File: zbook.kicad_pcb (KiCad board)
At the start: 2 copper layers, 157 parts, among them J1 USB_C_Receptacle_USB2.0_16P, J2 B2B-XH-A, J3 USB_C_Receptacle_USB2.0_16P, J4 Conn_01x03_Pin, J5 Conn_01x05_Pin, J6 MSD-4-A, J7 DISPLAY CONN, Q1 Q_NMOS_GSD, Q2 SL2301S, Q3 T2N7002AK,LM, SW1 SW_SPDT, SW2 SW_SPST, SW3 SW_SPST, SW4 SW_Push, SW5 SW_Push, SW6 SW_Push, SW7 SW_Push, U3 RP2040, U5 W25Q16JVSS, U6 W25Q16JVSS, U7 TSDP343xx, U8 GSDA213, Y1 12MHz/10pF, Y2 12MHz/10pF

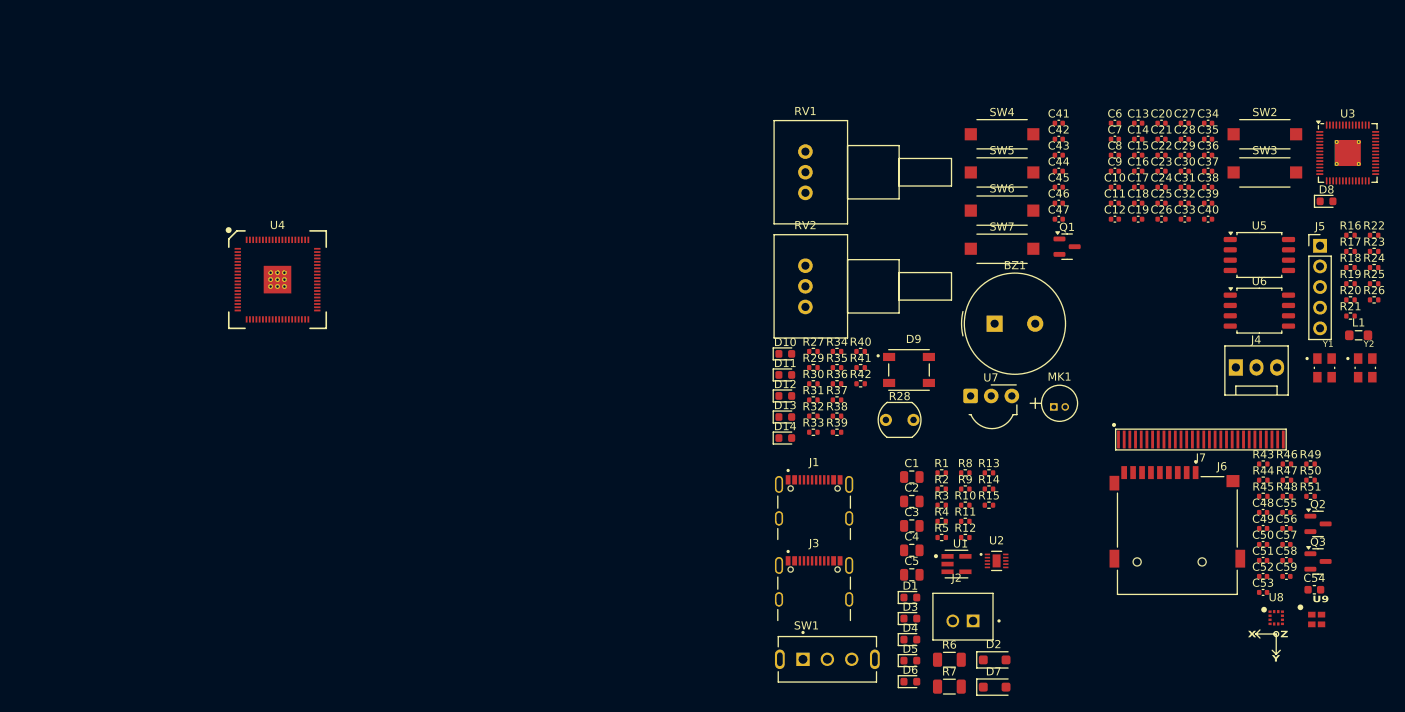
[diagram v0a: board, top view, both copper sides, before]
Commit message: feat: adds testpoints
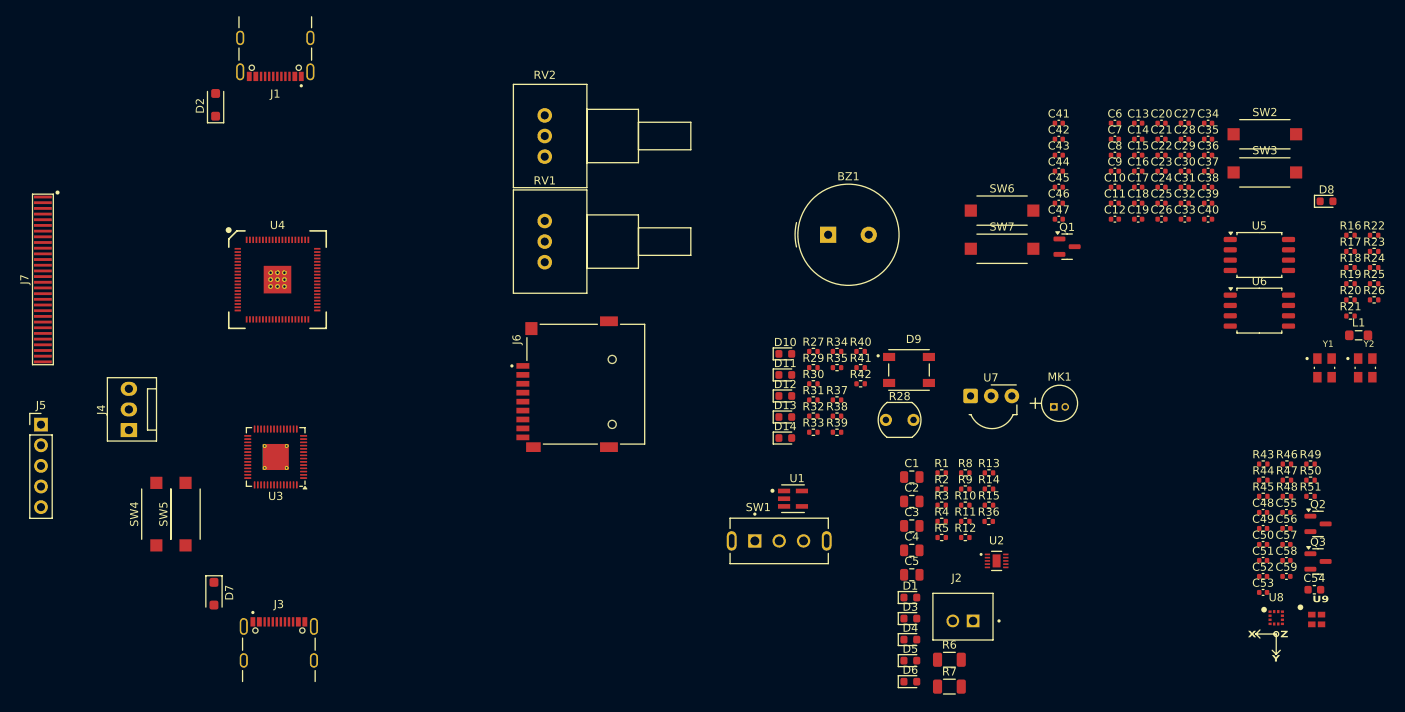
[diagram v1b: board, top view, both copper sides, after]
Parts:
- moved J5 159.0 mm to (111.8, 106.6)
- moved J7 143.9 mm to (112.0, 88.7), turned to -90 degrees
- moved U3 137.2 mm to (140.7, 110.6), turned to 180 degrees
- moved J4 136.5 mm to (122.6, 107.2), turned to 90 degrees
- moved D2 117.8 mm to (133.3, 67.2), turned to 90 degrees
- moved SW4 114.2 mm to (126.0, 117.6), turned to 90 degrees
- moved SW5 109.0 mm to (129.6, 117.6), turned to 90 degrees
- moved D7 96.8 mm to (133.1, 127.4), turned to -90 degrees
- moved J1 92.4 mm to (140.7, 56.4), turned to 180 degrees
- moved J6 75.2 mm to (178.9, 101.6), turned to 90 degrees
- moved J3 66.3 mm to (141.1, 138.2)
- moved RV2 37.1 mm to (173.8, 73.6)
- moved RV1 33.2 mm to (173.8, 86.6)
- moved R36 25.2 mm to (228.5, 118.5)
- moved BZ1 23.2 mm to (208.7, 83.2)
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
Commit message: wip: moves components around on PCB
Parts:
- added J6: Conn_02x10_Counter_Clockwise, Connector_PinSocket_2.54mm:PinSocket_2x10_P2.54mm_Vertical, F.Cu at (230.0, 122.5)
- added TP1: TestPoint_Small, TestPoint:TestPoint_Pad_D1.0mm, F.Cu at (331.6, 149.3)
- added TP10: TestPoint_Small, TestPoint:TestPoint_Pad_D1.0mm, F.Cu at (326.6, 155.4)
- added TP11: TestPoint_Small, TestPoint:TestPoint_Pad_D1.0mm, F.Cu at (326.6, 158.4)
- added TP12: TestPoint_Small, TestPoint:TestPoint_Pad_D1.0mm, F.Cu at (339.8, 163.5)
- added TP13: TestPoint_Small, TestPoint:TestPoint_Pad_D1.0mm, F.Cu at (331.6, 163.5)
- added TP14: TestPoint_Small, TestPoint:TestPoint_Pad_D1.0mm, F.Cu at (331.6, 166.6)
- added TP15: TestPoint_Small, TestPoint:TestPoint_Pad_D1.0mm, F.Cu at (331.6, 169.6)
- added TP16: TestPoint_Small, TestPoint:TestPoint_Pad_D1.0mm, F.Cu at (331.6, 172.7)
- added TP17: TestPoint_Small, TestPoint:TestPoint_Pad_D1.0mm, F.Cu at (334.7, 163.5)
- added TP18: TestPoint_Small, TestPoint:TestPoint_Pad_D1.0mm, F.Cu at (334.7, 166.6)
- added TP19: TestPoint_Small, TestPoint:TestPoint_Pad_D1.0mm, F.Cu at (334.7, 169.6)
- added TP2: TestPoint_Small, TestPoint:TestPoint_Pad_D1.0mm, F.Cu at (331.6, 152.3)
- added TP3: TestPoint_Small, TestPoint:TestPoint_Pad_D1.0mm, F.Cu at (331.6, 155.4)
- added TP4: TestPoint_Small, TestPoint:TestPoint_Pad_D1.0mm, F.Cu at (331.6, 158.4)
- added TP5: TestPoint_Small, TestPoint:TestPoint_Pad_D1.0mm, F.Cu at (334.7, 149.3)
- added TP6: TestPoint_Small, TestPoint:TestPoint_Pad_D1.0mm, F.Cu at (334.7, 152.3)
- added TP7: TestPoint_Small, TestPoint:TestPoint_Pad_D1.0mm, F.Cu at (334.7, 155.4)
- added TP8: TestPoint_Small, TestPoint:TestPoint_Pad_D1.0mm, F.Cu at (326.6, 149.3)
- added TP9: TestPoint_Small, TestPoint:TestPoint_Pad_D1.0mm, F.Cu at (326.6, 152.3)
- moved U8 162.1 mm to (108.2, 85.3)
- moved U9 158.1 mm to (119.5, 78.8), turned to 180 degrees
- moved J2 135.2 mm to (122.8, 42.2)
- moved R7 134.7 mm to (124.2, 48.0), turned to 180 degrees
- moved U6 132.4 mm to (132.0, 66.5), turned to 90 degrees
- moved R6 130.3 mm to (124.2, 51.3), turned to 180 degrees
- moved U2 125.0 mm to (124.4, 55.7)
- moved SW1 123.5 mm to (109.7, 39.8)
- moved Y1 122.9 mm to (147.0, 101.0), turned to 90 degrees
- moved SW2 119.9 mm to (147.5, 104.8)
- moved SW7 119.2 mm to (118.2, 125.8)
- moved U1 118.7 mm to (108.5, 45.8), turned to 180 degrees
- moved U5 117.4 mm to (152.0, 127.2), turned to -90 degrees
- moved R5 112.7 mm to (138.1, 46.0), turned to 180 degrees
- moved SW6 112.5 mm to (124.8, 119.7), turned to 90 degrees
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- renumbered J6 to J7, J7 to J8
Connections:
- U4 pad 18: unconnected-(U4-GPIO18-Pad18) -> GPIO18
- U4 pad 19: unconnected-(U4-GPIO19-Pad19) -> GPIO19
- U4 pad 27: unconnected-(U4-GPIO26-Pad27) -> GPIO26
- U4 pad 28: unconnected-(U4-GPIO27-Pad28) -> GPIO27
- U4 pad 3: unconnected-(U4-GPIO6-Pad3) -> GPIO06
- U4 pad 4: unconnected-(U4-GPIO7-Pad4) -> GPIO07
- U4 pad 55: unconnected-(U4-GPIO44_ADC4-Pad55) -> GPIO44
- U4 pad 56: unconnected-(U4-GPIO45_ADC5-Pad56) -> GPIO45
- U4 pad 57: unconnected-(U4-GPIO46_ADC6-Pad57) -> GPIO46
- U4 pad 58: unconnected-(U4-GPIO47_ADC7-Pad58) -> GPIO47
- U4 pad 6: unconnected-(U4-GPIO8-Pad6) -> GPIO08
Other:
- copper layers 2 -> 4

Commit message: feat:  adds requested components
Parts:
- added FID1: Fiducial, Fiducial:Fiducial_0.5mm_Mask1.5mm, F.Cu at (429.8, 128.3)
- added FID2: Fiducial, Fiducial:Fiducial_0.5mm_Mask1.5mm, F.Cu at (429.8, 131.3)
- added FID3: Fiducial, Fiducial:Fiducial_0.5mm_Mask1.5mm, F.Cu at (429.8, 134.4)
- added FID4: Fiducial, Fiducial:Fiducial_0.5mm_Mask1.5mm, F.Cu at (429.8, 137.4)
- added H1: MountingHole_Pad, MountingHole:MountingHole_2.5mm_Pad_Via, F.Cu at (425.0, 130.0)
- added H2: MountingHole_Pad, MountingHole:MountingHole_2.5mm_Pad_Via, F.Cu at (425.0, 136.6)
- added H3: MountingHole_Pad, MountingHole:MountingHole_2.5mm_Pad_Via, F.Cu at (425.0, 143.1)
- added H4: MountingHole_Pad, MountingHole:MountingHole_2.5mm_Pad_Via, F.Cu at (425.0, 149.7)
- added J4: Conn_01x03_Pin, Connector_PinHeader_2.54mm:PinHeader_1x03_P2.54mm_Vertical, F.Cu at (404.3, 129.1)
- added J6: Conn_02x04_Odd_Even, Connector_PinSocket_2.54mm:PinSocket_2x04_P2.54mm_Vertical, F.Cu at (414.1, 146.2)
- added Q1: Q_NMOS_GSD, Package_TO_SOT_SMD:SOT-23, F.Cu at (446.7, 130.4)
- added R27: 2.2K, Resistor_SMD:R_0402_1005Metric, F.Cu at (445.3, 135.6)
- added R49: 10k, Resistor_SMD:R_0402_1005Metric, F.Cu at (434.8, 155.4)
- added R51: 10k, Resistor_SMD:R_0402_1005Metric, F.Cu at (434.8, 157.4)
- added SW2: SW_Push, Button_Switch_THT:SW_PUSH_6mm_H4.3mm, F.Cu at (411.2, 128.8)
- added SW3: SW_Push, Button_Switch_THT:SW_PUSH_6mm_H4.3mm, F.Cu at (411.2, 137.3)
- added SW5: SW_Push, Button_Switch_THT:SW_PUSH_6mm_H4.3mm, F.Cu at (435.4, 128.8)
- added SW6: SW_Push, Button_Switch_THT:SW_PUSH_6mm_H4.3mm, F.Cu at (435.4, 137.3)
- added SW7: SW_Push, Button_Switch_THT:SW_PUSH_6mm_H4.3mm, F.Cu at (435.4, 145.9)
- C12: renamed from C37; value 15p -> 100n
- C15: renamed from C38; value 15p -> 100n
- C17: renamed from C8; value 4u7 -> 100n
- C18: renamed from C9; value 4u7 -> 100n
- C19: renamed from C33; value 100n -> 1u
- C20: renamed from C22; value 4u7 -> 1u
- C22: renamed from C23; value 100n -> 4u7
- C26: renamed from C29; value 15p -> 100n
- C27: renamed from C31; value 15p -> 100n
- C28: renamed from C20; value 1u -> 100n
- C29: renamed from C10; value 100n -> 15p
- C31: renamed from C19; value 1u -> 15p
- C37: renamed from C16; value 100n -> 15p
- C38: renamed from C17; value 100n -> 15p
- C42: renamed from C43; value 100n -> 1u
- C46: renamed from C42; value 1u -> 100n
- C47: value 100n -> 1u
- C48: renamed from C57; value 1u -> 100n
- C49: renamed from C58; value 1u -> 100n
- C51: renamed from C59; value 1u -> 100n
- C53: value 1u -> 2u2; footprint Capacitor_SMD:C_0402_1005Metric -> Capacitor_SMD:C_0603_1608Metric
- C54: renamed from C50; value 100n -> 1u
- C55: renamed from C54; value 2u2 -> 4u7; footprint Capacitor_SMD:C_0603_1608Metric -> Capacitor_SMD:C_0402_1005Metric
- C56: value 4u7 -> 1u
- C57: renamed from C51; value 100n -> 1u
- C58: renamed from C52; value 100n -> 1u
- C8: renamed from C32; value 100n -> 4u7
- C9: renamed from C35; value 100n -> 4u7
- D1: renamed from D2; value D_Schottky -> LED_GREEN; footprint Diode_SMD:D_SOD-123F -> LED_SMD:LED_0603_1608Metric
- D7: renamed from D6; value LED_GREEN -> D_Schottky; footprint LED_SMD:LED_0603_1608Metric -> Diode_SMD:D_SOD-123F
- J2: renamed from J3; value USB_C_Receptacle_USB2.0_16P -> B2B-XH-A; footprint power_supply:SAMESKY_UJ20-C-H-G-SMT-1-P16-TR -> B2B-XH-A:JST_B2B-XH-A
- J3: renamed from J2; value B2B-XH-A -> USB_C_Receptacle_USB2.0_16P; footprint B2B-XH-A:JST_B2B-XH-A -> power_supply:SAMESKY_UJ20-C-H-G-SMT-1-P16-TR
- J5: renamed from J4; value Conn_01x03_Pin -> Conn_01x05_Pin; footprint Connector:FanPinHeader_1x03_P2.54mm_Vertical -> Connector_PinHeader_2.54mm:PinHeader_1x05_P2.54mm_Vertical
- J6: value Conn_02x10_Counter_Clockwise -> Conn_02x04_Odd_Even; footprint Connector_PinSocket_2.54mm:PinSocket_2x10_P2.54mm_Vertical -> Connector_PinSocket_2.54mm:PinSocket_2x04_P2.54mm_Vertical
- J7: renamed from J5; value Conn_01x05_Pin -> Conn_02x15_Counter_Clockwise; footprint Connector_PinHeader_2.54mm:PinHeader_1x05_P2.54mm_Vertical -> Connector_PinHeader_2.54mm:PinHeader_2x15_P2.54mm_Vertical
- Q2: renamed from Q1; value Q_NMOS_GSD -> Q_Photo_NPN; footprint Package_TO_SOT_SMD:SOT-23 -> peripherals1:TO-18-2
- Q3: value T2N7002AK,LM -> SL2301S
- Q4: renamed from Q2; value SL2301S -> T2N7002AK,LM
- R1: renamed from R3; value 5.1k -> 1k
- R10: renamed from R4; value 1k -> 10k
- R11: renamed from R6; value 0R -> 1k; footprint Resistor_SMD:R_1206_3216Metric -> Resistor_SMD:R_0402_1005Metric
- R12: renamed from R7; value 0R -> 1k; footprint Resistor_SMD:R_1206_3216Metric -> Resistor_SMD:R_0402_1005Metric
- R14: renamed from R13; value 1k -> 5.1k
- R15: renamed from R2; value 10k -> 5.1k
- R16: renamed from R25; value 10k -> 1k
- R19: renamed from R26; value 10k -> 33R
- R2: renamed from R5; value 5.1k -> 10k
- R20: renamed from R19; value 33R -> 27R
- R22: renamed from R21; value 27R -> 1k
- R25: renamed from R22; value 1k -> 10k
- R26: renamed from R24; value 1k -> 10k
- R28: renamed from R32; value 220 -> R_Photo; footprint Resistor_SMD:R_0402_1005Metric -> OptoDevice:R_LDR_5.1x4.3mm_P3.4mm_Vertical
- R29: renamed from R37; value 220 -> 10k
- R30: renamed from R38; value 220 -> 10k
- R31: renamed from R40; value 220 -> 10k
- R32: renamed from R29; value 10k -> 220
- R35: renamed from R42; value 27 -> 1k
- R36: renamed from R30; value 10k -> 500
- R37: renamed from R34; value 10k -> 220
- R38: renamed from R27; value 2.2K -> 220
- R39: renamed from R35; value 1k -> 500
- R4: renamed from R15; value 5.1k -> 1k
- R40: renamed from R28; value R_Photo -> 220; footprint OptoDevice:R_LDR_5.1x4.3mm_P3.4mm_Vertical -> Resistor_SMD:R_0402_1005Metric
- R42: renamed from R36; value 500 -> 27
- R43: renamed from R39; value 500 -> 10k
- R44: value 10k -> 4k7
- R45: renamed from R50; value 10k -> 4k7
- R46: renamed from R49; value 560k -> 4k7
- R47: renamed from R48; value 10k -> 4k7
- R48: renamed from R51; value 10k -> 4k7
- R5: renamed from R10; value 10k -> 5.1k
- R50: renamed from R45; value 4k7 -> 560k
- R52: renamed from R46; value 4k7 -> 10k
- R6: renamed from R8; value 20k -> 0R; footprint Resistor_SMD:R_0402_1005Metric -> Resistor_SMD:R_1206_3216Metric
- R7: renamed from R9; value 1k -> 0R; footprint Resistor_SMD:R_0402_1005Metric -> Resistor_SMD:R_1206_3216Metric
- R8: renamed from R11; value 1k -> 20k
- SW2, SW3: value SW_SPST -> SW_Push; footprint microcontroller:SMD Button -> Button_Switch_THT:SW_PUSH_6mm_H4.3mm
- SW4, SW5, SW6, SW7: footprint microcontroller:SMD Button -> Button_Switch_THT:SW_PUSH_6mm_H4.3mm
- U1: renamed from U2; footprint power_supply:WSON10_DLH_TEX -> power_supply:DBV0005A-IPC_B
- U2: renamed from U1; footprint power_supply:DBV0005A-IPC_B -> power_supply:WSON10_DLH_TEX
- U3: renamed from U5; value W25Q16JVSS -> RP2040; footprint Package_SO:SOIC-8_5.3x5.3mm_P1.27mm -> Package_DFN_QFN:QFN-56-1EP_7x7mm_P0.4mm_EP3.2x3.2mm_ThermalVias
- U6: renamed from U3; value RP2040 -> W25Q16JVSS; footprint Package_DFN_QFN:QFN-56-1EP_7x7mm_P0.4mm_EP3.2x3.2mm_ThermalVias -> Package_SO:SOIC-8_5.3x5.3mm_P1.27mm
- U7: renamed from U9; value ~ -> GSDA213; footprint peripherals2:LTR-329ALS-01_LTO-M -> peripherals2:LGA12_GAS-M
- U7: value TSDP343xx -> GSDA213; footprint OptoDevice:Vishay_MOLD-3Pin -> peripherals2:LGA12_GAS-M
- U8: value GSDA213 -> ~; footprint peripherals2:LGA12_GAS-M -> peripherals2:LTR-329ALS-01_LTO-M
- moved U5 79.5 mm to (166.2, 138.2)
- moved U6 46.8 mm to (132.0, 72.8)
- moved SW5 5.13 mm to (122.2, 110.2), turned to 180 degrees
- moved J5 4.83 mm to (97.7, 106.0)
- moved SW6 4.30 mm to (120.5, 119.8)
- moved SW7 4.29 mm to (122.2, 127.2), turned to 180 degrees
- moved SW4 0.10 mm to (113.0, 119.8)
- renumbered C5 to C1, C36 to C10, C6 to C11, C39 to C13, C34 to C14, C7 to C16, C4 to C2, C40 to C21, C30 to C23, C27 to C25, C1 to C3, C18 to C30, C11 to C32, C12 to C33, C13 to C34, C14 to C35, C15 to C36, C21 to C39, C2 to C4, C25 to C40, C45 to C43, C46 to C45, C48 to C47, C3 to C5, C49 to C50, C55 to C52, C26 to C6, C28 to C7, D7 to D2, D4 to D3, D1 to D4, D3 to D5, D5 to D6, J7 to J8, J8 to J9, R12 to R13, R20 to R21, R16 to R24, R14 to R3, R41 to R34, R31 to R41, R47 to R44, R1 to R9, TP5 to TP1, TP19 to TP13, TP18 to TP15, TP15 to TP18, TP13 to TP19, TP7 to TP2, TP6 to TP4, TP4 to TP5, TP1 to TP6, TP2 to TP7, U6 to U5, Y2 to Y1, Y1 to Y2
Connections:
- C1 pad 1: +BATT -> +VBQ
- C10 pad 1: +3V3 -> +1V1
- C12 pad 1: Net-(U4-XIN) -> +3V3
- C14 pad 1: +1V1 -> +3V3
- C15 pad 1: Net-(U4-XOUT) -> +3V3
- C17 pad 1: +1V1 -> +3V3
- C18 pad 1: +3V3 -> +1V1
- C2 pad 1: +VBQ -> +3V3
- C20 pad 1: Net-(U4-VREG_AVDD) -> GND
- C20 pad 2: GND -> +1V1
- C21 pad 1: +3V3 -> /Microcontroller/RUN_RP2350
- C22 pad 1: +3V3 -> Net-(U4-VREG_AVDD)
- C25 pad 1: +1V1 -> /Microcontroller/RUN_RP2040
- C26 pad 1: Net-(U3-XIN) -> +3V3
- C27 pad 1: Net-(C31-Pad1) -> +1V1
- C28 pad 1: GND -> +3V3
- C28 pad 2: +1V1 -> GND
- C29 pad 1: +1V1 -> Net-(U3-XIN)
- C3 pad 1: +VBQ -> +VBUS
- C30 pad 1: +1V1 -> +3V3
- C31 pad 1: +3V3 -> Net-(C31-Pad1)
- C34 pad 1: +3V3 -> +1V1
- C37 pad 1: +3V3 -> Net-(U4-XIN)
- C38 pad 1: +3V3 -> Net-(U4-XOUT)
- C39 pad 1: /Microcontroller/RUN_RP2350 -> +3V3
- C4 pad 1: +3V3 -> +VBQ
- C40 pad 1: /Microcontroller/RUN_RP2040 -> +3V3
- C42 pad 1: BUTTON1_GPIO -> Net-(MK1--)
- C42 pad 2: GND -> MICROPHONE_ADC
- C43 pad 1: BUTTON3_GPIO -> BUTTON1_GPIO
- C45 pad 1: BUTTON4_GPIO -> BUTTON3_GPIO
- C46 pad 1: Net-(MK1--) -> BUTTON4_GPIO
- C46 pad 2: MICROPHONE_ADC -> GND
- C5 pad 1: +VBUS -> +BATT
- C51 pad 1: +V_DISP -> +3V3
- C52 pad 1: Net-(J8-C1P) -> Net-(J9-C2P)
- C52 pad 2: Net-(J8-C1N) -> Net-(J9-C2N)
- C53 pad 1: Net-(J8-C2P) -> Net-(J9-VCC)
- C53 pad 2: Net-(J8-C2N) -> GND
- C54 pad 1: +3V3 -> Net-(J9-C1P)
- C54 pad 2: GND -> Net-(J9-C1N)
- C55 pad 1: Net-(J8-VCC) -> Net-(J9-VCOMH)
- C56 pad 1: Net-(J8-VCOMH) -> +3V3
- C58 pad 1: +3V3 -> +V_DISP
- C8 pad 1: +3V3 -> +1V1
- D1 pad 1: +VBUS -> Net-(D1-K)
- D1 pad 2: Net-(D2-A) -> +VBQ
- D2 pad 2: Net-(D7-A) -> Net-(D2-A)
- D3 pad 1: Net-(D4-K) -> Net-(D3-K)
- D3 pad 2: +VBUS -> +VBQ
- D4 pad 1: Net-(D1-K) -> Net-(D4-K)
- D4 pad 2: +VBQ -> +VBUS
- D5 pad 1: Net-(D3-K) -> Net-(D5-K)
- D6 pad 2: +VBQ -> +3V3
- D7 pad 1: Net-(D6-K) (its old number) -> +VBUS
- D7 pad 2: +3V3 -> Net-(D7-A)
- J5 pad 1: /Microcontroller/SWDIO_RP2040 -> /Microcontroller/RP2350_TX/BT_WIFI_RX
- J5 pad 2: /Microcontroller/SWCLK_RP2040 -> /Microcontroller/RP2350_RX/BT_WIFI_TX
- J6 pad 1: GPIO06 -> GND
- J6 pad 2: GPIO07 -> /Microcontroller/RP2350_RX/BT_WIFI_TX
- J6 pad 3: GPIO08 -> unconnected-(J6-Pin_3-Pad3)
- J6 pad 4: GPIO18 -> /Microcontroller/WIFI_EN
- J6 pad 5: GPIO47 -> unconnected-(J6-Pin_5-Pad5)
- J6 pad 6: GPIO46 -> /Microcontroller/WIFI_RST
- J6 pad 7: GPIO45 -> /Microcontroller/RP2350_TX/BT_WIFI_RX
- J6 pad 8: GPIO44 -> +3V3
- J7 pad 1: /Microcontroller/RP2350_TX/BT_RX -> /Microcontroller/GPIO06
- J7 pad 2: /Microcontroller/RP2350_RX/BT_TX -> /Microcontroller/GPIO07
- J7 pad 3: GND -> /Microcontroller/GPIO08
- J7 pad 4: +3V3 -> /Microcontroller/GPIO26
- J7 pad 5: Net-(J5-Pin_5) -> /Microcontroller/GPIO27
- J9 pad 2: Net-(J8-C2P) -> Net-(J9-C2P)
- J9 pad 26: Net-(J8-IREF) -> Net-(J9-IREF)
- J9 pad 27: Net-(J8-VCOMH) -> Net-(J9-VCOMH)
- J9 pad 28: Net-(J8-VCC) -> Net-(J9-VCC)
- J9 pad 3: Net-(J8-C2N) -> Net-(J9-C2N)
- J9 pad 4: Net-(J8-C1P) -> Net-(J9-C1P)
- J9 pad 5: Net-(J8-C1N) -> Net-(J9-C1N)
- Q2 pad 1: MOSFET_GPIO -> +3V3
- Q2 pad 2: GND -> IR_REC_GPIO
- Q3 pad 1: DISPLAY_EN -> Net-(Q3-G)
- Q3 pad 2: GND -> +V_DISP
- Q3 pad 3: Net-(Q2-G) -> +3V3
- Q4 pad 1: Net-(Q2-G) -> DISPLAY_EN
- Q4 pad 2: +V_DISP -> GND
- Q4 pad 3: +3V3 -> Net-(Q3-G)
- R1 pad 1: Net-(J1-CC1) -> /Power Supply/STAT1
- R1 pad 2: GND -> Net-(D1-K)
- R10 pad 1: /Power Supply/STAT2 -> GND
- R10 pad 2: Net-(D3-K) -> Net-(U2-TS/MR)
- R11 pad 1: +VBUS -> GND
- R11 pad 2: +VBQ -> Net-(D4-K)
- R12 pad 1: +VBUS -> GND
- R12 pad 2: +VBQ -> Net-(D5-K)
- R14 pad 1: GND -> Net-(J3-CC1)
- R14 pad 2: Net-(D6-K) (its old number) -> GND
- R15 pad 1: /Power Supply/LDO_EN -> Net-(J3-CC2)
- R15 pad 2: +VBQ -> GND
- R16 pad 1: +3V3 -> /Microcontroller/RUN_RP2350
- R16 pad 2: /Microcontroller/QSPI_SS_RP2040 -> +3V3
- R19 pad 1: +3V3 -> Net-(U4-VREG_AVDD)
- R19 pad 2: /Microcontroller/QSPI_SS_RP2350 -> +3V3
- R2 pad 1: Net-(J1-CC2) -> /Power Supply/LDO_EN
- R2 pad 2: GND -> +VBQ
- R20 pad 1: Net-(U4-VREG_AVDD) -> USB_PROBE_D+
- R20 pad 2: +3V3 -> Net-(U3-USB_DP)
- R21 pad 1: USB_PROBE_D+ -> USB_PROBE_D-
- R21 pad 2: Net-(U3-USB_DP) -> Net-(U3-USB_DM)
- R22 pad 1: USB_PROBE_D- -> /Microcontroller/RUN_RP2040
- R22 pad 2: Net-(U3-USB_DM) -> +3V3
- R24 pad 1: /Microcontroller/RUN_RP2350 -> Net-(D8-K)
- R24 pad 2: +3V3 -> Net-(J5-Pin_5)
- R25 pad 1: /Microcontroller/RUN_RP2040 -> +3V3
- R25 pad 2: +3V3 -> /Microcontroller/QSPI_SS_RP2040
- R26 pad 1: Net-(D8-K) -> +3V3
- R26 pad 2: Net-(J5-Pin_5) -> /Microcontroller/QSPI_SS_RP2350
- R28 pad 1: ~{LED_GREEN_GPIO} -> +3V3
- R28 pad 2: Net-(D10-K) -> LDR_ADC
- R29 pad 1: ~{LED_RED_GPIO} -> BUTTON1_GPIO
- R29 pad 2: Net-(D11-K) -> +3V3
- R3 pad 1: Net-(J3-CC1) -> Net-(J1-CC1)
- R30 pad 1: ~{LED_YELLOW_GPIO} -> BUTTON2_GPIO
- R30 pad 2: Net-(D12-K) -> +3V3
- R31 pad 1: ~{LED_BLUE_GPIO} -> LDR_ADC
- R31 pad 2: Net-(D13-K) -> GND
- R32 pad 1: BUTTON1_GPIO -> ~{LED_GREEN_GPIO}
- R32 pad 2: +3V3 -> Net-(D10-K)
- R34 pad 1: MOSFET_GPIO -> BUTTON4_GPIO
- R34 pad 2: GND -> +3V3
- R35 pad 1: ~{IR_EMITTER_GPIO} -> BUZZER_GPIO
- R35 pad 2: Net-(D14-K) -> Net-(BZ1-+)
- R36 pad 1: BUTTON2_GPIO -> Net-(R36-Pad1)
- R36 pad 2: +3V3 -> POTENTIOMETER1_ADC
- R37 pad 1: BUTTON4_GPIO -> ~{LED_RED_GPIO}
- R37 pad 2: +3V3 -> Net-(D11-K)
- R38 pad 1: +3V3 -> ~{LED_YELLOW_GPIO}
- R38 pad 2: Net-(MK1--) -> Net-(D12-K)
- R39 pad 1: BUZZER_GPIO -> Net-(R39-Pad1)
- R39 pad 2: Net-(BZ1-+) -> POTENTIOMETER2_ADC
- R4 pad 1: Net-(J3-CC2) -> /Power Supply/STAT2
- R4 pad 2: GND -> Net-(D3-K)
- R40 pad 1: +3V3 -> ~{LED_BLUE_GPIO}
- R40 pad 2: LDR_ADC -> Net-(D13-K)
- R41 pad 1: LDR_ADC -> MOSFET_GPIO
- R42 pad 1: Net-(R36-Pad1) -> ~{IR_EMITTER_GPIO}
- R42 pad 2: POTENTIOMETER1_ADC -> Net-(D14-K)
- R43 pad 1: +3V3 -> GND
- R43 pad 2: I2C_SDA -> IR_REC_GPIO
- R43 pad 1: Net-(R39-Pad1) -> GND
- R43 pad 2: POTENTIOMETER2_ADC -> IR_REC_GPIO
- R44 pad 1: SD_CD/DAT3 -> I2C_SDA
- R44 pad 1: +3V3 -> I2C_SDA
- R44 pad 2: I2C_SCL -> +3V3
- R45 pad 1: +3V3 -> I2C_SCL
- R45 pad 2: ~{DISPLAY_RST} -> +3V3
- R46 pad 1: Net-(J8-IREF) -> SPI_SCLK
- R46 pad 2: GND -> +3V3
- R47 pad 1: +3V3 -> SPI_MOSI
- R47 pad 2: Net-(Q2-G) -> +3V3
- R48 pad 1: DISPLAY_EN -> SD_CD/DAT3
- R48 pad 2: GND -> +3V3
- R5 pad 1: GND -> Net-(J1-CC2)
- R5 pad 2: Net-(U2-TS/MR) -> GND
- R50 pad 1: SPI_SCLK -> Net-(J9-IREF)
- R50 pad 2: +3V3 -> GND
- R52 pad 1: SPI_MOSI -> DISPLAY_EN
- R52 pad 2: +3V3 -> GND
- R6 pad 1: GND -> +VBUS
- R6 pad 2: Net-(U2-ILIM/VSET) -> +VBQ
- R7 pad 1: GND -> +VBUS
- R7 pad 2: Net-(U2-ISET) -> +VBQ
- R8 pad 2: Net-(D4-K) -> Net-(U2-ILIM/VSET)
- R9 pad 1: /Power Supply/STAT1 -> GND
- R9 pad 2: Net-(D1-K) -> Net-(U2-ISET)
- TP1 pad 1: GND -> +VBQ
- TP13 pad 1: DISPLAY_EN -> SPI_MISO
- TP14 pad 1: SPI_MISO -> I2C_SDA
- TP15 pad 1: +V_DISP -> I2C_SCL
- TP16 pad 1: I2C_SDA -> SPI_MOSI
- TP17 pad 1: I2C_SCL -> SPI_SCLK
- TP18 pad 1: SPI_MOSI -> +V_DISP
- TP19 pad 1: SPI_SCLK -> DISPLAY_EN
- TP2 pad 1: GND -> +3V3
- TP4 pad 1: +VBUS -> +BATT
- TP5 pad 1: +BATT -> GND
- TP6 pad 1: +VBQ -> +VBUS
- TP7 pad 1: +3V3 -> GND
- U1 pad 2: +BATT -> GND
- U1 pad 3: /Power Supply/STAT2 -> /Power Supply/LDO_EN
- U1 pad 4: GND -> unconnected-(U1-NC-Pad4)
- U1 pad 5: GND -> +3V3
- U2 pad 2: GND -> +BATT
- U2 pad 3: /Power Supply/LDO_EN -> /Power Supply/STAT2
- U2 pad 4: unconnected-(U1-NC-Pad4) -> GND
- U2 pad 5: +3V3 -> GND
- U3 pad 1: /Microcontroller/QSPI_SS_RP2040 -> +3V3
- U3 pad 2: /Microcontroller/QSPI_SD1_RP2040 -> unconnected-(U3-GPIO0-Pad2)
- U3 pad 3: /Microcontroller/QSPI_SD2_RP2040 -> unconnected-(U3-GPIO1-Pad3)
- U3 pad 4: GND -> /Microcontroller/SWCLK
- U3 pad 5: /Microcontroller/QSPI_SD0_RP2040 -> /Microcontroller/SWDIO
- U3 pad 6: /Microcontroller/QSPI_SCLK_RP2040 -> /Microcontroller/RP2350_RX/RP2040_TX
- U3 pad 7: /Microcontroller/QSPI_SD3_RP2040 -> /Microcontroller/RP2350_TX/RP2040_RX
- U3 pad 8: +3V3 -> unconnected-(U3-GPIO6-Pad8)
- U4 pad 18: GPIO18 -> /Microcontroller/WIFI_RST
- U4 pad 19: GPIO19 -> /Microcontroller/WIFI_EN
- U4 pad 27: GPIO26 -> /Microcontroller/GPIO26
- U4 pad 28: GPIO27 -> /Microcontroller/GPIO27
- U4 pad 3: GPIO06 -> /Microcontroller/GPIO06
- U4 pad 4: GPIO07 -> /Microcontroller/GPIO07
- U4 pad 55: GPIO44 -> /Microcontroller/GPIO45
- U4 pad 56: GPIO45 -> /Microcontroller/GPIO45
- U4 pad 57: GPIO46 -> /Microcontroller/GPIO46
- U4 pad 58: GPIO47 -> /Microcontroller/GPIO47
- U4 pad 6: GPIO08 -> /Microcontroller/GPIO08
- U5 pad 1: /Microcontroller/QSPI_SS_RP2350 -> /Microcontroller/QSPI_SS_RP2040
- U5 pad 2: /Microcontroller/QSPI_SD1_RP2350 -> /Microcontroller/QSPI_SD1_RP2040
- U5 pad 3: /Microcontroller/QSPI_SD2_RP2350 -> /Microcontroller/QSPI_SD2_RP2040
- U5 pad 5: /Microcontroller/QSPI_SD0_RP2350 -> /Microcontroller/QSPI_SD0_RP2040
- U5 pad 6: /Microcontroller/QSPI_SCLK_RP2350 -> /Microcontroller/QSPI_SCLK_RP2040
- U5 pad 7: /Microcontroller/QSPI_SD3_RP2350 -> /Microcontroller/QSPI_SD3_RP2040
- U6 pad 1: +3V3 -> /Microcontroller/QSPI_SS_RP2350
- U6 pad 2: unconnected-(U3-GPIO0-Pad2) -> /Microcontroller/QSPI_SD1_RP2350
- U6 pad 3: unconnected-(U3-GPIO1-Pad3) -> /Microcontroller/QSPI_SD2_RP2350
- U6 pad 4: /Microcontroller/SWCLK -> GND
- U6 pad 5: /Microcontroller/SWDIO -> /Microcontroller/QSPI_SD0_RP2350
- U6 pad 6: /Microcontroller/RP2350_RX/RP2040_TX -> /Microcontroller/QSPI_SCLK_RP2350
- U6 pad 7: /Microcontroller/RP2350_TX/RP2040_RX -> /Microcontroller/QSPI_SD3_RP2350
- U6 pad 8: unconnected-(U3-GPIO6-Pad8) -> +3V3
- U7 pad 1: +3V3 -> SPI_MISO
- U7 pad 2: GND -> SPI_MOSI (x2)
- U7 pad 3: I2C_SDA -> +3V3
- U7 pad 4: I2C_SCL -> unconnected-(U7-NC-Pad4)
- U7 pad 1: IR_REC_GPIO -> SPI_MISO
- U8 pad 1: SPI_MISO -> +3V3
- U8 pad 2: SPI_MOSI -> GND
- U8 pad 3: +3V3 -> I2C_SDA
- U8 pad 4: unconnected-(U8-NC-Pad4) -> I2C_SCL
- Y1 pad 1: Net-(U4-XIN) -> Net-(U3-XIN)
- Y1 pad 3: Net-(U4-XOUT) -> Net-(C31-Pad1)
- Y2 pad 1: Net-(U3-XIN) -> Net-(U4-XIN)
- Y2 pad 3: Net-(C31-Pad1) -> Net-(U4-XOUT)
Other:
- rule pad_to_mask_clearance: 0 -> 0.052

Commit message: chore: resets PCB and adds constraints
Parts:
- removed the C47 at (367.0, 108.9)
- removed the C47 at (341.8, 72.8)
- removed the J6 at (414.1, 146.2)
- removed the J6 at (230.0, 122.5)
- removed the R43 at (367.0, 102.9)
- removed the R43 at (314.5, 99.0)
- removed the R44 at (369.9, 104.9)
- removed the R44 at (367.0, 104.9)
- removed the SW2 at (147.5, 104.8)
- removed the SW2 at (411.2, 128.8)
- removed the SW3 at (367.2, 67.0)
- removed the SW3 at (411.2, 137.3)
- removed the SW5 at (435.4, 128.8)
- removed the SW5 at (122.2, 110.2)
- removed the SW6 at (120.5, 119.8)
- removed the SW6 at (435.4, 137.3)
- removed the SW7 at (122.2, 127.2)
- removed the SW7 at (435.4, 145.9)
- removed the U7 at (119.5, 78.8)
- removed the U7 at (331.0, 94.5)
- added C47: 1u, Capacitor_SMD:C_0402_1005Metric, F.Cu at (359.1, 106.9)
- added J6: Conn_02x04_Odd_Even, Connector_PinSocket_2.54mm:PinSocket_2x04_P2.54mm_Vertical, F.Cu at (398.7, 87.1)
- added R43: 10k, Resistor_SMD:R_0402_1005Metric, F.Cu at (366.6, 98.1)
- added R44: 4k7, Resistor_SMD:R_0402_1005Metric, F.Cu at (357.9, 119.1)
- added SW2: SW_Push, Button_Switch_THT:SW_PUSH_6mm_H4.3mm, F.Cu at (385.3, 58.9)
- added SW3: SW_Push, Button_Switch_THT:SW_PUSH_6mm_H4.3mm, F.Cu at (385.3, 67.5)
- added SW5: SW_Push, Button_Switch_THT:SW_PUSH_6mm_H4.3mm, F.Cu at (358.5, 67.5)
- added SW6: SW_Push, Button_Switch_THT:SW_PUSH_6mm_H4.3mm, F.Cu at (358.5, 76.0)
- added SW7: SW_Push, Button_Switch_THT:SW_PUSH_6mm_H4.3mm, F.Cu at (358.5, 84.6)
- added U7: GSDA213, peripherals2:LGA12_GAS-M, F.Cu at (359.5, 126.2)
- moved J7 305.1 mm to (378.4, 59.2)
- moved SW1 299.5 mm to (398.8, 118.1)
- moved J5 289.4 mm to (385.6, 76.3), turned to 0 degrees
- moved R12 283.9 mm to (395.9, 130.7), turned to 0 degrees
- moved U2 282.5 mm to (378.7, 128.2), turned to 0 degrees
- moved R11 282.4 mm to (395.9, 128.7), turned to 0 degrees
- moved U6 281.1 mm to (413.0, 67.2), turned to 0 degrees
- moved U1 274.4 mm to (389.0, 128.0)
- moved D1 271.8 mm to (398.0, 100.4)
- moved J3 269.9 mm to (381.7, 118.2)
- moved J9 268.8 mm to (345.3, 103.9), turned to 0 degrees
- moved R2 266.8 mm to (393.0, 124.7), turned to 0 degrees
- moved U3 265.9 mm to (412.8, 75.6), turned to 0 degrees
- moved R1 261.9 mm to (393.0, 122.7)
- moved U4 261.1 mm to (400.8, 63.9)
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
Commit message: wip: microcontroller placement
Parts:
- moved C35 149.7 mm to (350.4, 212.6), turned to -90 degrees
- moved C34 148.3 mm to (361.1, 213.0), turned to -90 degrees
- moved C36 147.1 mm to (352.4, 212.6), turned to -90 degrees
- moved C37 144.4 mm to (354.7, 212.5), turned to -90 degrees
- moved C38 143.1 mm to (359.2, 214.8), turned to -90 degrees
- moved U4 143.1 mm to (356.9, 200.1)
- moved C22 135.3 mm to (385.8, 210.3)
- moved C28 135.3 mm to (388.7, 208.4)
- moved C26 135.3 mm to (385.8, 218.2)
- moved C32 135.3 mm to (388.7, 216.2)
- moved C6 135.3 mm to (380.1, 206.4)
- moved C7 135.3 mm to (380.1, 208.4)
- moved C8 135.3 mm to (380.1, 210.3)
- moved C9 135.3 mm to (380.1, 212.3)
- moved L1 135.3 mm to (370.6, 229.7)
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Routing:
- net Net-(U4-XOUT): track 0.00 -> 1.44 mm

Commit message: wip: places rp circuitry
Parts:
- added R53: 1k, Resistor_SMD:R_0402_1005Metric, F.Cu at (360.1, 211.1)
- moved U5 144.9 mm to (320.1, 171.6)
- moved U6 132.7 mm to (349.5, 183.7), turned to -90 degrees
- moved C29 127.9 mm to (398.0, 203.6), turned to -90 degrees
- moved C31 126.1 mm to (402.4, 205.9), turned to -90 degrees
- moved C18 122.0 mm to (405.5, 203.6), turned to -90 degrees
- moved U3 121.8 mm to (402.6, 197.0)
- moved R25 121.3 mm to (315.0, 169.2), turned to -90 degrees
- moved C14 120.9 mm to (408.1, 194.4)
- moved C20 119.9 mm to (408.1, 191.6), turned to 180 degrees
- moved C39 119.7 mm to (323.7, 168.1), turned to 90 degrees
- moved C13 118.8 mm to (402.9, 190.6), turned to 90 degrees
- moved C40 116.6 mm to (353.0, 187.3)
- moved C15 116.6 mm to (422.9, 189.8)
- moved C16 116.6 mm to (422.9, 191.8)
- moved C17 116.6 mm to (422.9, 193.8)
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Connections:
- C38 pad 1: Net-(U4-XOUT) -> Net-(C38-Pad1)
- Y2 pad 3: Net-(U4-XOUT) -> Net-(C38-Pad1)
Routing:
- net Net-(U3-XIN): track 0.00 -> 5.49 mm
- net Net-(U3-XOUT): track 0.00 -> 3.10 mm
- net Net-(C31-Pad1): track 0.00 -> 3.03 mm
- net Net-(C38-Pad1): track 0.00 -> 3.03 mm
- net Net-(U4-XOUT): track 1.44 -> 0.00 mm
- net GND: track 0.00 -> 1.28 mm, vias 0 -> 1
- net +3V3: track 0.00 -> 0.55 mm
